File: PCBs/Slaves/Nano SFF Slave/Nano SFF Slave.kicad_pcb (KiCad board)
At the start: 2 copper layers, 56 x 50 mm, 65 parts, among them J1 Screw_Terminal_01x02, J10 AVR-ISP-6, J11 Conn_01x06_Female, J12 Screw_Terminal_01x02, J13 Screw_Terminal_01x02, J14 Screw_Terminal_01x02, J15 Screw_Terminal_01x02, J16 Screw_Terminal_01x02, J2 Screw_Terminal_01x02, J3 Screw_Terminal_01x02, J4 Screw_Terminal_01x02, J5 Screw_Terminal_01x02, J6 Screw_Terminal_01x02, J7 Screw_Terminal_01x02, J8 Screw_Terminal_01x02, J9 Screw_Terminal_01x02, SW1 SW_DIP_x02, SW2 SW_DIP_x02, SW3 SW_MEC_5E, U1 ATmega328P-AU, U10 TISP4240M3BJR-S, U2 MAX487ESA+T, U3 ULN2003A, U4 MAX487CPA+, U5 AMS1117-5.0, U6 HY15P03C2, U7 TBU-CA065-200-WH, U8 TBU-CA065-200-WH, U9 TISP4240M3BJR-S, Y1 Crystal_GND24

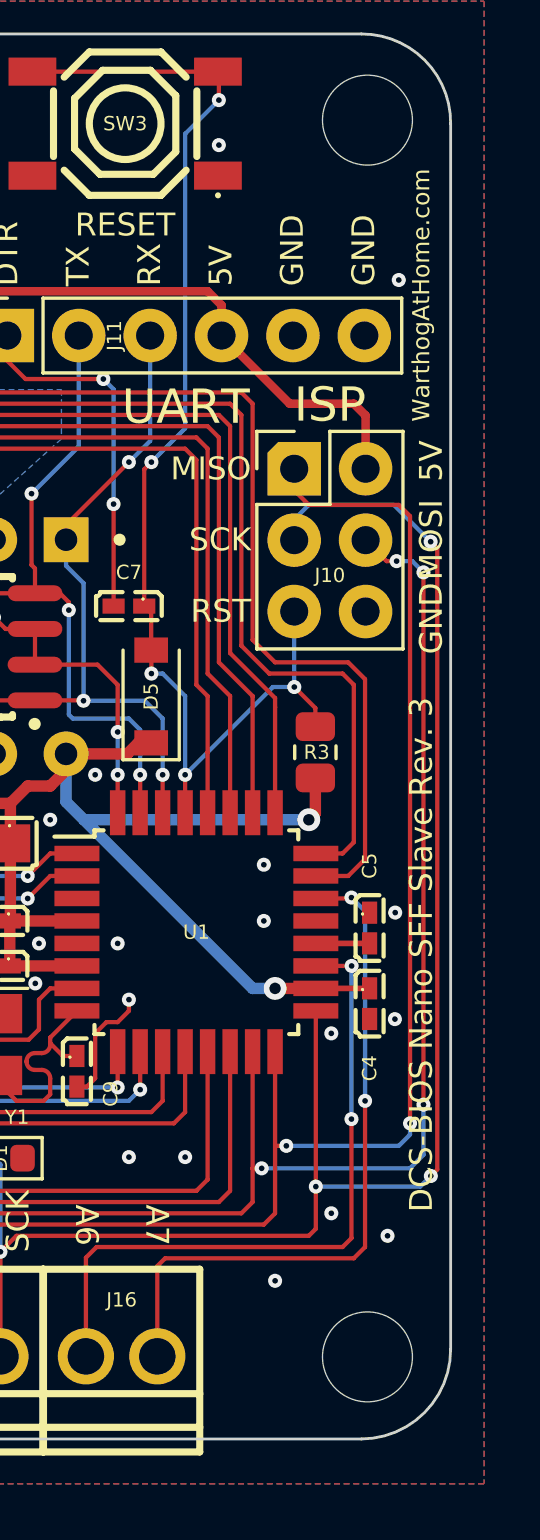
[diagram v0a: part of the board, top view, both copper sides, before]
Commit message: Updated Nano SFF Revision and date information
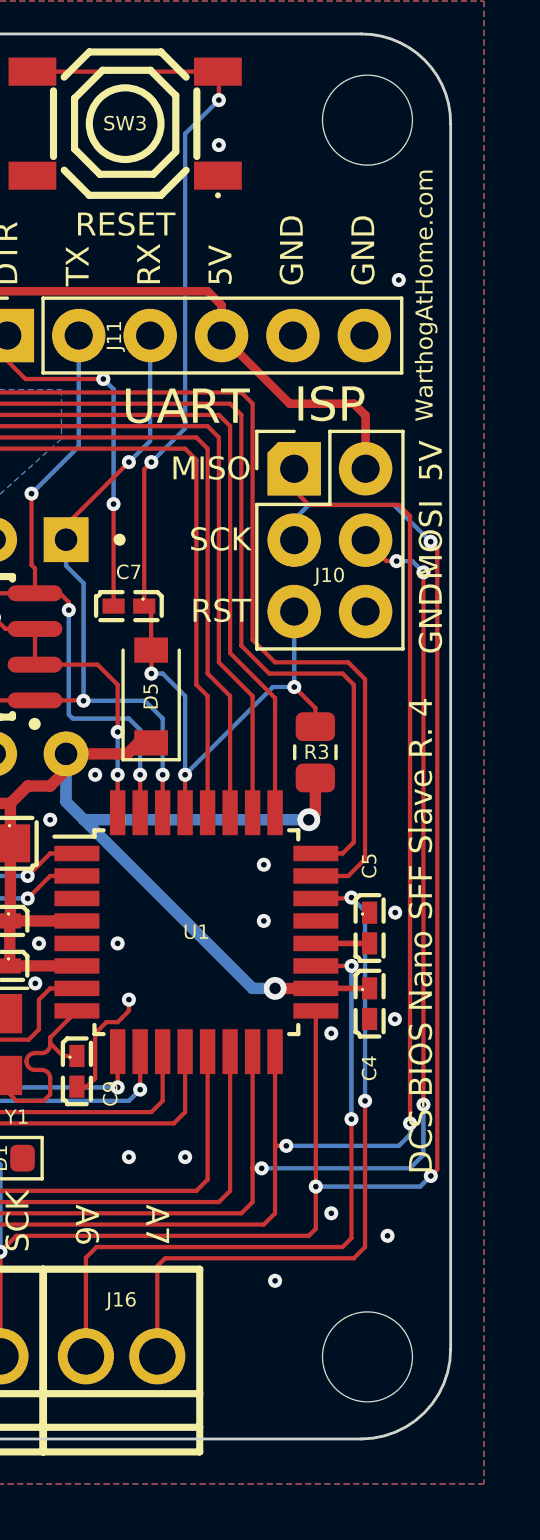
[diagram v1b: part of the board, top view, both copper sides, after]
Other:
- board text added: "${TITLE} R. ${REVISION}"
- board text removed: "${TITLE} Rev. ${REVISION}"
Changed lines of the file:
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@@
   (title_block
     (title "DCS-BIOS Nano SFF Slave")
-    (date "2022-12-15")
-    (rev "3")
+    (date "2022-12-29")
+    (rev "4")
   )
   (layers
@@
     (effects (font (size 0.9652 0.9652) (thickness 0.1778)))
   )
-  (gr_text "${TITLE} Rev. ${REVISION}" (at 153.628292 103.52826 90) (layer "F.SilkS")
+  (gr_text "${TITLE} R. ${REVISION}" (at 153.628292 103.52826 90) (layer "F.SilkS")
     (effects (font (size 0.8128 0.8128) (thickness 0.127)) (justify right))
   )
@@
     (effects (font (size 0.9652 0.9652) (thickness 0.1778)))
   )
-  (gr_text "WarthogAtHome.com" (at 153.628292 84.72591 90) (layer "F.SilkS")
+  (gr_text "WarthogAtHome.com" (at 153.75 84.72591 90) (layer "F.SilkS")
     (effects (font (size 0.6096 0.6096) (thickness 0.1016)) (justify right))
   )

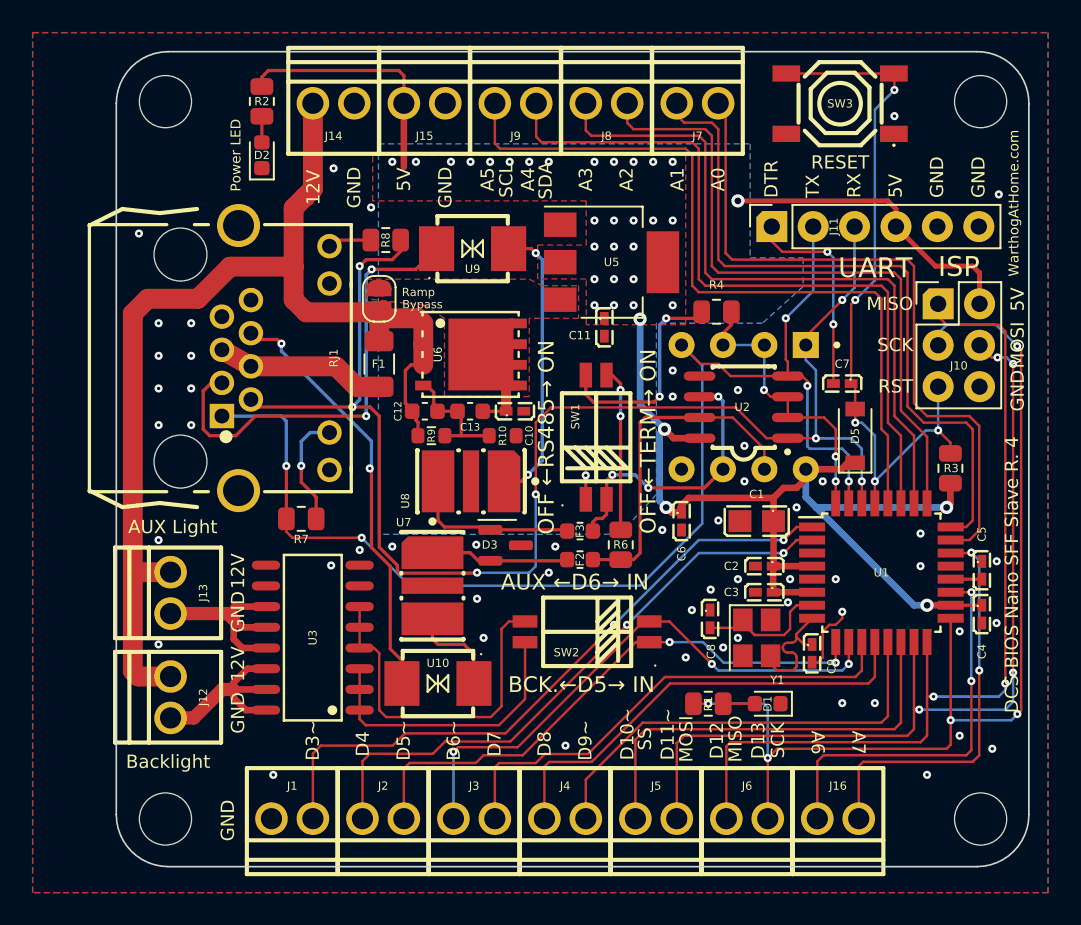
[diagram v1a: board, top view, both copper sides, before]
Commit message: Removed voltage ramp and some protection from Nano SFF Slave
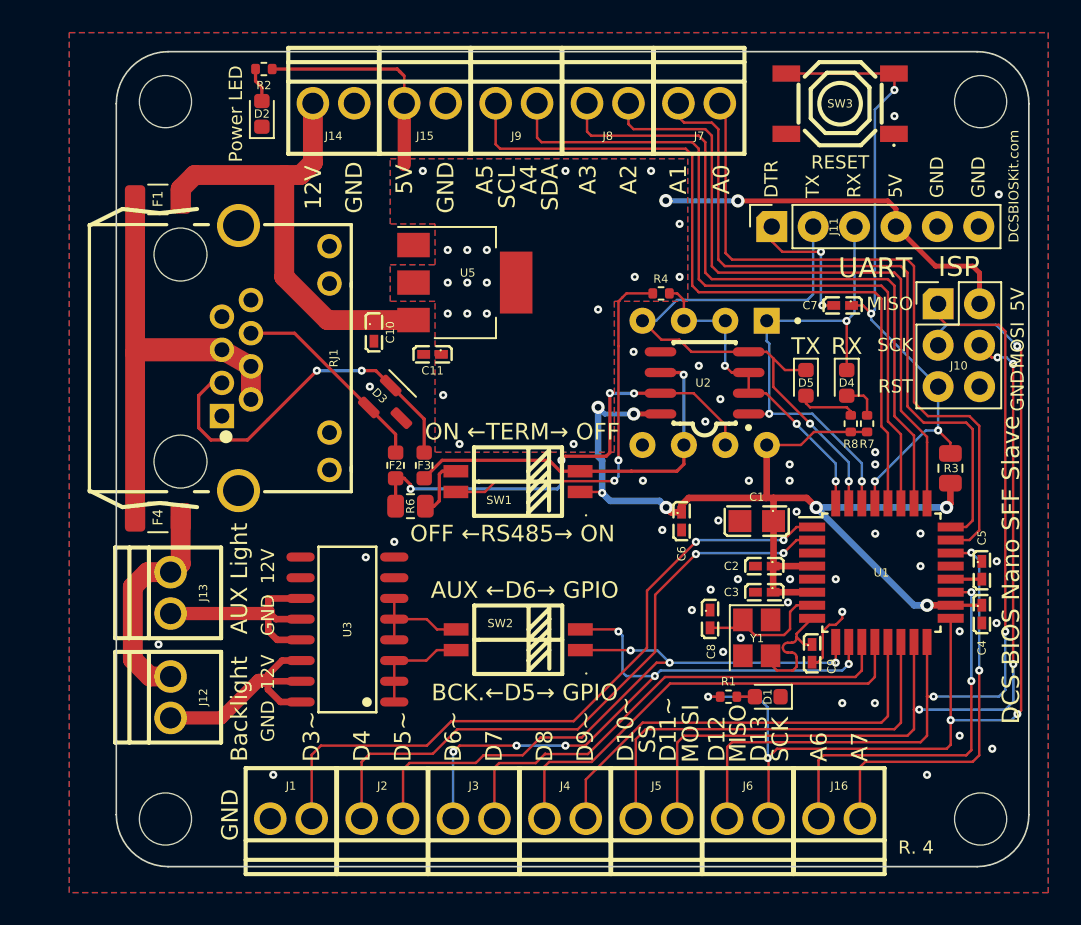
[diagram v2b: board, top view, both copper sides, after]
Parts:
- removed C12: 470nF, Capacitor_SMD:C_0603_1608Metric
- removed C13: 47nF, Capacitor_SMD:C_0603_1608Metric
- removed JP1: Solder, Jumper:SolderJumper-2_P1.3mm_Open_RoundedPad1.0x1.5mm
- removed R10: 1M, Resistor_SMD:R_0603_1608Metric
- removed R9: 10M, Resistor_SMD:R_0603_1608Metric
- removed U10, U9: TISP4240M3BJR-S, A10 KiCad Libraries:DO-214AA_L4.4-W3.6-LS5.3-BI
- removed U6: HY15P03C2, A10 KiCad Libraries:DFN-8_L5.9-W5.2-P1.27-LS6.2-BL
- removed U7, U8: TBU-CA065-200-WH, A10 KiCad Libraries:DIO-SMD_3P-L6.5-W4.0-BI
- added D4: LED, LED_SMD:LED_0603_1608Metric, F.Cu at (143.5, 100.2)
- added F4: 500mA, Fuse:Fuse_1206_3216Metric, F.Cu at (101.2, 108.5)
- D5: value 1N4148W -> LED; footprint Diode_SMD:D_SOD-123 -> LED_SMD:LED_0603_1608Metric
- R1, R2: value 1.5K -> 1K; footprint Resistor_SMD:R_0805_2012Metric -> Resistor_SMD:R_0402_1005Metric
- R4: footprint Resistor_SMD:R_0805_2012Metric -> Resistor_SMD:R_0402_1005Metric
- R7, R8: value 1.8K -> 1K; footprint Resistor_SMD:R_0805_2012Metric -> Resistor_SMD:R_0402_1005Metric
- moved R7 35.2 mm to (144.8, 102.8), turned to -90 degrees
- moved R8 30.7 mm to (143.8, 102.8), turned to -90 degrees
- moved F1 16.9 mm to (101.2, 89.0), turned to 180 degrees
- moved R6 13.1 mm to (116.7, 107.8), turned to 0 degrees
- moved F2 12.7 mm to (115.8, 105.3), turned to 90 degrees
- moved D3 11.0 mm to (115.5, 101.8), turned to -45 degrees
- moved C11 10.7 mm to (118.1, 98.5), turned to 180 degrees
- moved F3 10.4 mm to (117.6, 105.3), turned to -90 degrees
- moved C10 9.91 mm to (114.5, 97.1), turned to -90 degrees
- moved U5 9.09 mm to (120.1, 94.1)
- moved SW1 5.51 mm to (123.3, 106.3), turned to 90 degrees
- moved C7 4.79 mm to (143.2, 95.5)
- moved D5 4.44 mm to (141.0, 100.2), turned to -90 degrees
- moved SW2 4.25 mm to (123.4, 116.0)
- moved R4 3.58 mm to (132.1, 94.8)
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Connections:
- C10 pad 1: 12V_Ramped -> 12V_Fused_MCU
- D3 pad 1: Net-(D3-Pad1) -> RS485+
- D3 pad 2: Net-(D3-Pad2) -> RS485-
- D5 pad 1: +5V -> TXD
- D5 pad 2: RESET -> Net-(D5-Pad2)
- F1 pad 1: 12V_Fused -> 12V_Fused_MCU
- F2 pad 2: Net-(D3-Pad2) -> RS485-
- F3 pad 1: Net-(D3-Pad1) -> RS485+
- J12 pad 2: 12V_Fused -> 12V_Fused_LED
- J13 pad 2: 12V_Fused -> 12V_Fused_LED
- J14 pad 1: 12V_Fused -> 12V_Fused_MCU
- R7 pad 1: Net-(R7-Pad1) -> Net-(D4-Pad2)
- R7 pad 2: TXD -> +5V
- R8 pad 1: Net-(R8-Pad1) -> Net-(D5-Pad2)
- R8 pad 2: RXD -> +5V
- RJ1 pad 1: TXD -> GND
- RJ1 pad 10: Net-(R7-Pad1) -> GND
- RJ1 pad 12: Net-(R8-Pad1) -> GND
- RJ1 pad 2: RXD -> +12V
- U5 pad 3: 12V_Ramped -> 12V_Fused_MCU
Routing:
- net 12V_Fused: track 69.0 -> 0.00 mm
- net RXD: track 87.4 -> 30.3 mm, vias 7 -> 3
- net TXD: track 79.1 -> 37.4 mm, vias 5 -> 2
- net 12V_Fused_MCU: track 0.00 -> 28.3 mm
- net +12V: track 10.4 -> 28.7 mm
- net Net-(U8-Pad1): track 17.5 -> 0.00 mm, vias 2 -> 0
- net AUX_BASE: track 21.7 -> 6.60 mm
- net 12V_Fused_LED: track 0.00 -> 13.6 mm
- net RS485-: track 26.1 -> 12.6 mm, vias 2 -> 0
- net BACKLIGHT_BASE: track 17.6 -> 6.60 mm
- net Net-(D3-Pad1): track 10.6 -> 0.00 mm
- net Net-(R4-Pad1): track 13.4 -> 23.4 mm
- net TERM_B: track 20.9 -> 29.8 mm, vias 0 -> 4
- net Net-(D3-Pad2): track 8.50 -> 0.00 mm
- net Net-(C12-Pad2): track 7.42 -> 0.00 mm
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- removed copper zone on F.Cu, net 12V_Ramped
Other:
- board text added: "${TITLE}"
- board text added: "AUX ←D6→ GPIO"
- board text added: "BCK.←D5→ GPIO"
- board text added: "DCSBIOSKit.com"
- board text added: "ON ←TERM→ OFF"
- board text added: "R. ${REVISION}"
- board text removed: "${TITLE} R. ${REVISION}"
- board text removed: "AUX ←D6→ IN"
- board text removed: "BCK.←D5→ IN"
- board text removed: "OFF ←TERM→ ON"
- board text removed: "WarthogAtHome.com"

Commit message: Updated Nano SFF Slave
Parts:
- added G***: LOGO, LOGO, B.Cu at (136.0, 86.0)
- added G***: LOGO, LOGO, B.Cu at (106.0, 87.5)
- added G***: LOGO, LOGO, B.Cu at (124.0, 125.5)
- added G***: LOGO, LOGO, B.Cu at (142.8, 114.2)
- added R10: 3.6K, Resistor_SMD:R_0603_1608Metric, F.Cu at (114.2, 94.0)
- added R9: 1K, Resistor_SMD:R_0402_1005Metric, F.Cu at (114.0, 103.8)
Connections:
- RJ1 pad 10: GND -> Net-(R9-Pad2)
- RJ1 pad 12: GND -> Net-(R10-Pad2)
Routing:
- net +5V: track 105.4 -> 112.3 mm, vias 28 -> 29
- net Net-(R10-Pad2): track 0.00 -> 3.02 mm
- net Net-(R9-Pad2): track 0.00 -> 2.22 mm
- net 12V_Fused_MCU: track 28.3 -> 29.5 mm
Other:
- board text added: "44MM→"
- board text added: "WARNING! DO NOT CONNECT TO HOME NETWORK! DO NOT HOTPLUG!"
- board text added: "←50MM"
- board text removed: "44MM →"
- board text removed: "50MM →"
- board text removed: "BRRRRRRRRT"
